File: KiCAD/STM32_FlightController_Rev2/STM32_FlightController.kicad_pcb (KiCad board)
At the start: 4 copper layers, 42 x 44.4 mm, 56 parts, among them J1 629105150521, J2 JST_SH_SM08B-SRSS-TB_1x08-1MP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, J3 JST_SH_SM04B-SRSS-TB_1x04-1MP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, J4 JST_SH_SM04B-SRSS-TB_1x04-1MP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, J5 Conn_02x05_Odd_Even, SW1 PTS815SJM250SMTRLFS, SW2 PCM12SMTR, U1 SN74LVC1T45DBV, U2 ICM-20948, U3 STM32F405RGTx, U4 USBLC6-2SC6, U5 AMS1117-3.3, U6 TLV70018, U7 BMP390L, U8 SN74LVC1T45DBV, Y1 X32258MOB4SI

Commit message: final edits, passed DRC
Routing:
- net GND: track 64.5 -> 66.8 mm, vias 71 -> 72
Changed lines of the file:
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@@
 	)
 	(segment
+		(start 107.08 61.405)
+		(end 107.075 61.4)
+		(width 0.3)
+		(layer "F.Cu")
+		(net 1)
+	)
+	(segment
 		(start 106.65 72.9225)
 		(end 106.6375 72.91)
@@
 	)
 	(segment
+		(start 107.08 62.26)
+		(end 107.08 61.405)
+		(width 0.3)
+		(layer "F.Cu")
+		(net 1)
+	)
+	(segment
 		(start 109.95 60.52)
 		(end 110.455 60.52)
@@
 	)
 	(segment
-		(start 106.099451 61.599451)
-		(end 106.298902 61.4)
-		(width 0.3)
-		(layer "F.Cu")
-		(net 1)
-	)
-	(segment
 		(start 111.75 62.8)
 		(end 111.75 61.825)
@@
 	)
 	(segment
-		(start 106.298902 61.4)
-		(end 107.075 61.4)
-		(width 0.3)
-		(layer "F.Cu")
-		(net 1)
-	)
-	(segment
 		(start 111.313299 48.986701)
 		(end 110.85 49.45)
@@
 	)
 	(via
+		(at 117.13 76.73)
+		(size 0.6)
+		(drill 0.3)
+		(layers "F.Cu" "B.Cu")
+		(net 1)
+	)
+	(via
 		(at 114.975 55.85)
 		(size 0.6)
@@
 	)
 	(via
-		(at 106.099451 61.599451)
+		(at 107.08 62.26)
 		(size 0.6)
 		(drill 0.3)
@@
 	)
 	(segment
+		(start 115.55 79.625)
+		(end 115.505 79.625)
+		(width 0.3)
+		(layer "B.Cu")
+		(net 1)
+	)
+	(segment
 		(start 110.35 67.0625)
 		(end 110.35 68.9875)
@@
 	)
 	(segment
+		(start 118.55 76.725)
+		(end 117.135 76.725)
+		(width 0.5)
+		(layer "B.Cu")
+		(net 1)
+	)
+	(segment
 		(start 109.5875 69.7875)
 		(end 109.55 69.7875)
@@
 	)
 	(segment
+		(start 115.55 79.625)
+		(end 114.475 79.625)
+		(width 0.3)
+		(layer "B.Cu")
+		(net 1)
+	)
+	(segment
 		(start 111.6 55.825)
 		(end 111.625 55.85)
@@
 	)
 	(segment
+		(start 117.135 76.725)
+		(end 117.13 76.73)
+		(width 0.5)
+		(layer "B.Cu")
+		(net 1)
+	)
+	(segment
 		(start 111.525 47.025)
 		(end 110.86 47.025)
@@
 	)
 	(segment
-		(start 119.8 63.275)
-		(end 120.275 63.75)
-		(width 0.2)
-		(layer "F.Cu")
-		(net 3)
-	)
-	(segment
 		(start 108.7 61.475)
 		(end 108.625 61.4)
@@
 	)
 	(segment
+		(start 121 62.66)
+		(end 121.64 62.66)
+		(width 0.2)
+		(layer "F.Cu")
+		(net 3)
+	)
+	(segment
 		(start 105.05 70.6375)
 		(end 105.0625 70.625)
@@
 	)
 	(via
-		(at 119.8 63.275)
+		(at 123.15 76.6)
 		(size 0.6)
 		(drill 0.3)
@@
 	)
 	(via
-		(at 123.15 76.6)
+		(at 121.64 62.66)
 		(size 0.6)
 		(drill 0.3)
@@
 		(start 123.256249 65.3)
 		(end 123.806249 64.75)
-		(width 0.15)
+		(width 0.16)
 		(layer "F.Cu")
 		(net 13)
@@
 		(start 123.806249 64.75)
 		(end 124.7 64.75)
-		(width 0.15)
+		(width 0.16)
 		(layer "F.Cu")
 		(net 13)
@@
 	)
 	(segment
-		(start 124.7 64.75)
-		(end 124.75 64.8)
-		(width 0.15)
-		(layer "F.Cu")
-		(net 13)
-	)
-	(segment
-		(start 124.75 64.8)
-		(end 124.975 64.575)
-		(width 0.1)
-		(layer "F.Cu")
-		(net 13)
-	)
-	(segment
 		(start 123.781249 66.275)
 		(end 124.725 66.275)
-		(width 0.15)
-		(layer "F.Cu")
-		(net 14)
-	)
-	(segment
-		(start 124.725 66.275)
-		(end 124.75 66.25)
-		(width 0.15)
+		(width 0.16)
 		(layer "F.Cu")
 		(net 14)
@@
 		(start 123.256249 65.75)
 		(end 123.781249 66.275)
-		(width 0.15)
-		(layer "F.Cu")
-		(net 14)
-	)
-	(segment
-		(start 124.75 66.25)
-		(end 124.975 66.475)
-		(width 0.1)
+		(width 0.16)
 		(layer "F.Cu")
 		(net 14)
@@
 		(polygon
 			(pts
-				(xy 115 79.025) (xy 114.75 79.275) (xy 114.75 79.975) (xy 115 80.225) (xy 120.15 80.225) (xy 120.45 80.525)
+				(xy 115 79.025) (xy 114.76 79.265) (xy 114.76 79.985) (xy 115 80.225) (xy 120.15 80.225) (xy 120.45 80.525)
 				(xy 121.15 80.525) (xy 121.4 80.275) (xy 121.4 79.175) (xy 121.15 78.925) (xy 119.85 78.925) (xy 119.65 78.725)
 				(xy 119.65 76.175) (xy 119.35 75.875) (xy 117.75 75.875) (xy 117.45 76.175) (xy 117.45 78.725) (xy 117.15 79.025)
@@
 		(layer "B.Cu")
 		(hatch edge 0.5)
-		(priority 2)
+		(priority 8)
 		(connect_pads yes
 			(clearance 0.3)
@@
 		(polygon
 			(pts
-				(xy 113.3 77.3) (xy 113.3 74.2) (xy 114.2 74.2) (xy 114.25 74.148387) (xy 114.25 73.625) (xy 114.175 73.55)
-				(xy 112.787519 73.55) (xy 112.1 74.283354) (xy 112.1 77.3)
+				(xy 115.85 84.525) (xy 115.85 81.925) (xy 113.3 79.375) (xy 113.3 74.35) (xy 113.45 74.2) (xy 114.2 74.2)
+				(xy 114.25 74.148387) (xy 114.25 73.625) (xy 114.175 73.55) (xy 112.787519 73.55) (xy 112.1 74.283354)
+				(xy 112.1 79.61) (xy 115.15 82.7) (xy 115.15 84.525)
 			)
 		)
@@
 			)
 		)
-	)
-	(zone
-		(net 8)
-		(net_name "+5V")
-		(layer "B.Cu")
-		(hatch edge 0.5)
-		(priority 9)
-		(connect_pads yes
-			(clearance 0.3)
-		)
-		(min_thickness 0.25)
-		(filled_areas_thickness no)
-		(fill yes
-			(thermal_gap 0.5)
-			(thermal_bridge_width 0.5)
-		)
-		(polygon
-			(pts
-				(xy 113.3 77.3) (xy 113.3 79.375) (xy 115.85 81.925) (xy 115.85 84.525) (xy 115.15 84.525) (xy 115.15 82.7)
-				(xy 112.068666 79.618666) (xy 112.1 77.3)
-			)
-		)

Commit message: added manufacturing related files
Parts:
- moved C13 84.5 mm to (41.7, 45.1)
- moved C7 84.5 mm to (27.6, 42.4)
- moved J1 84.5 mm to (52.9, 35.5)
- moved C10 84.5 mm to (28.5, 22.3)
- moved C11 84.5 mm to (34.1, 20.4)
- moved C12 84.5 mm to (32.0, 24.6)
- moved C14 84.5 mm to (43.8, 31.7)
- moved C16 84.5 mm to (42.3, 24.5)
- moved C17 84.5 mm to (31.3, 39.8)
- moved C18 84.5 mm to (31.5, 32.7)
- moved C2 84.5 mm to (31.0, 31.0)
- moved C21 84.5 mm to (25.2, 35.4)
- moved C22 84.5 mm to (25.2, 37.7)
- moved C23 84.5 mm to (26.8, 29.0)
- moved C3 84.5 mm to (42.0, 32.1)
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
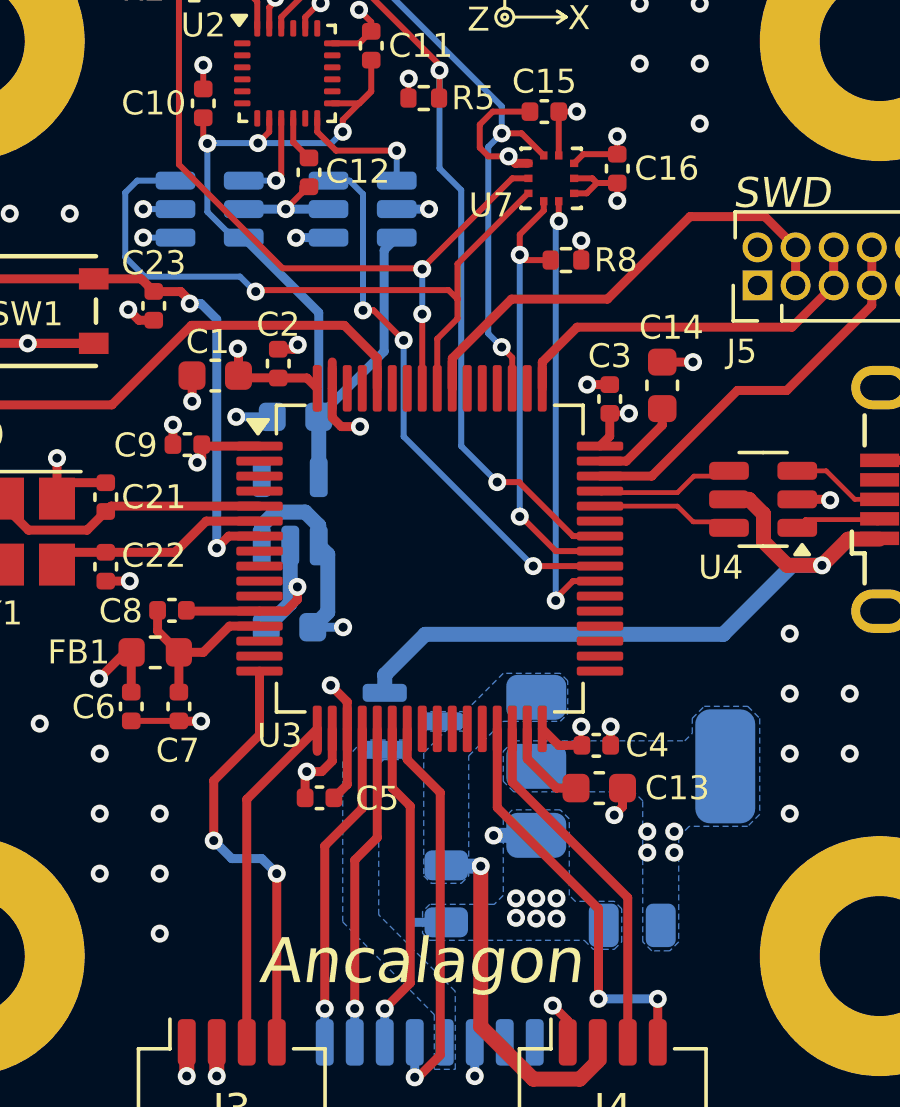
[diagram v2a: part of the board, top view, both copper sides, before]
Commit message: added some draw rule areas for GND planes
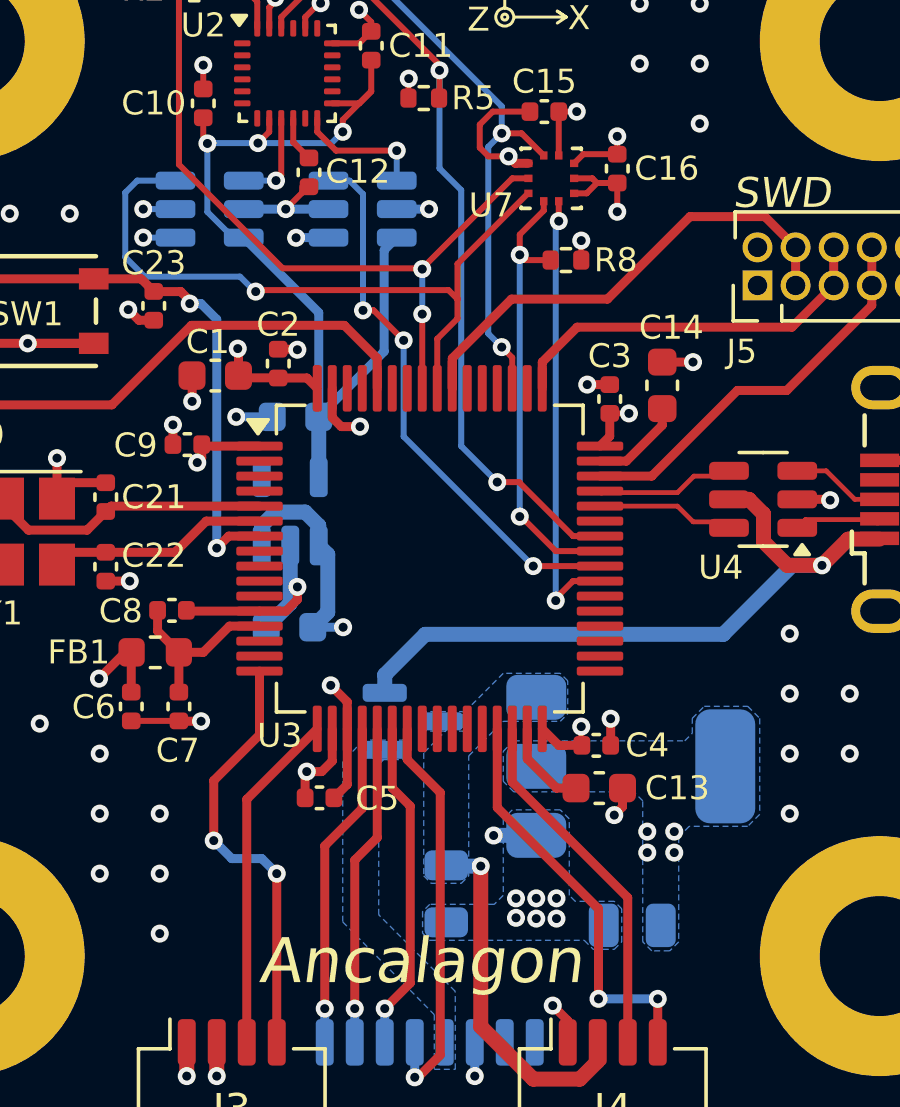
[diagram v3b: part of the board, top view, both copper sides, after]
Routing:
- net GND: track 66.8 -> 65.4 mm
- net /GPS_TX: track 12.2 -> 11.4 mm

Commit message: aesthetics changes
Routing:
- net GND: track 65.4 -> 59.3 mm
